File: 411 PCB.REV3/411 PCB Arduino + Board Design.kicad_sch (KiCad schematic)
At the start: 27 parts, among them J1 ICSP CONN, J3 Conn_01x04, J4 HEADER-1X770MIL, Q1 Q_NMOS_GDS, SW1 SW_SPST, SW2 SW_MEC_5E, U2 ATmega328P-P, Y1 8 MHz

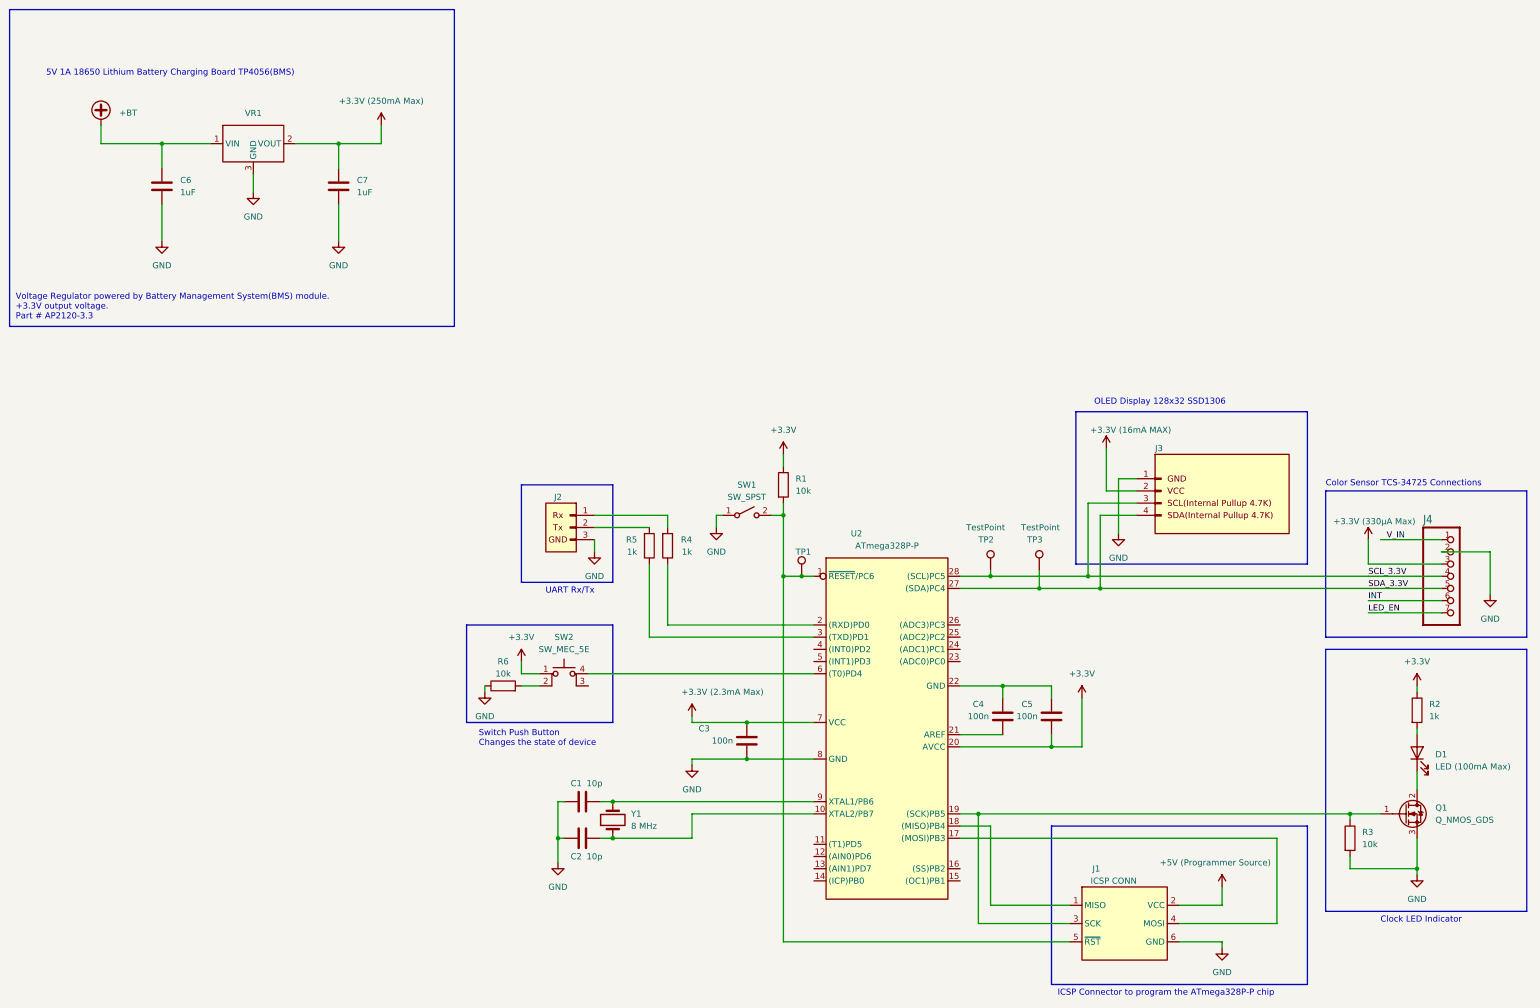
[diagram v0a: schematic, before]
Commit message: EEPROM, Debounce, more testpoints (#2)
* Create RGB_sensor_project.ino

Arduino projector, getting basics of the color sensor and display working (together).

* Removed RGB LED code and cleaned up code

* added LED connection for RGB Sensor

* starting to incorporate EEPROM

* Added EEPROM code and changed the pins for button and RGB Sensors LED. Also changed how the chip goes into calibration mode

* pins that work

* Fixed debounce error and added more test points to schematic
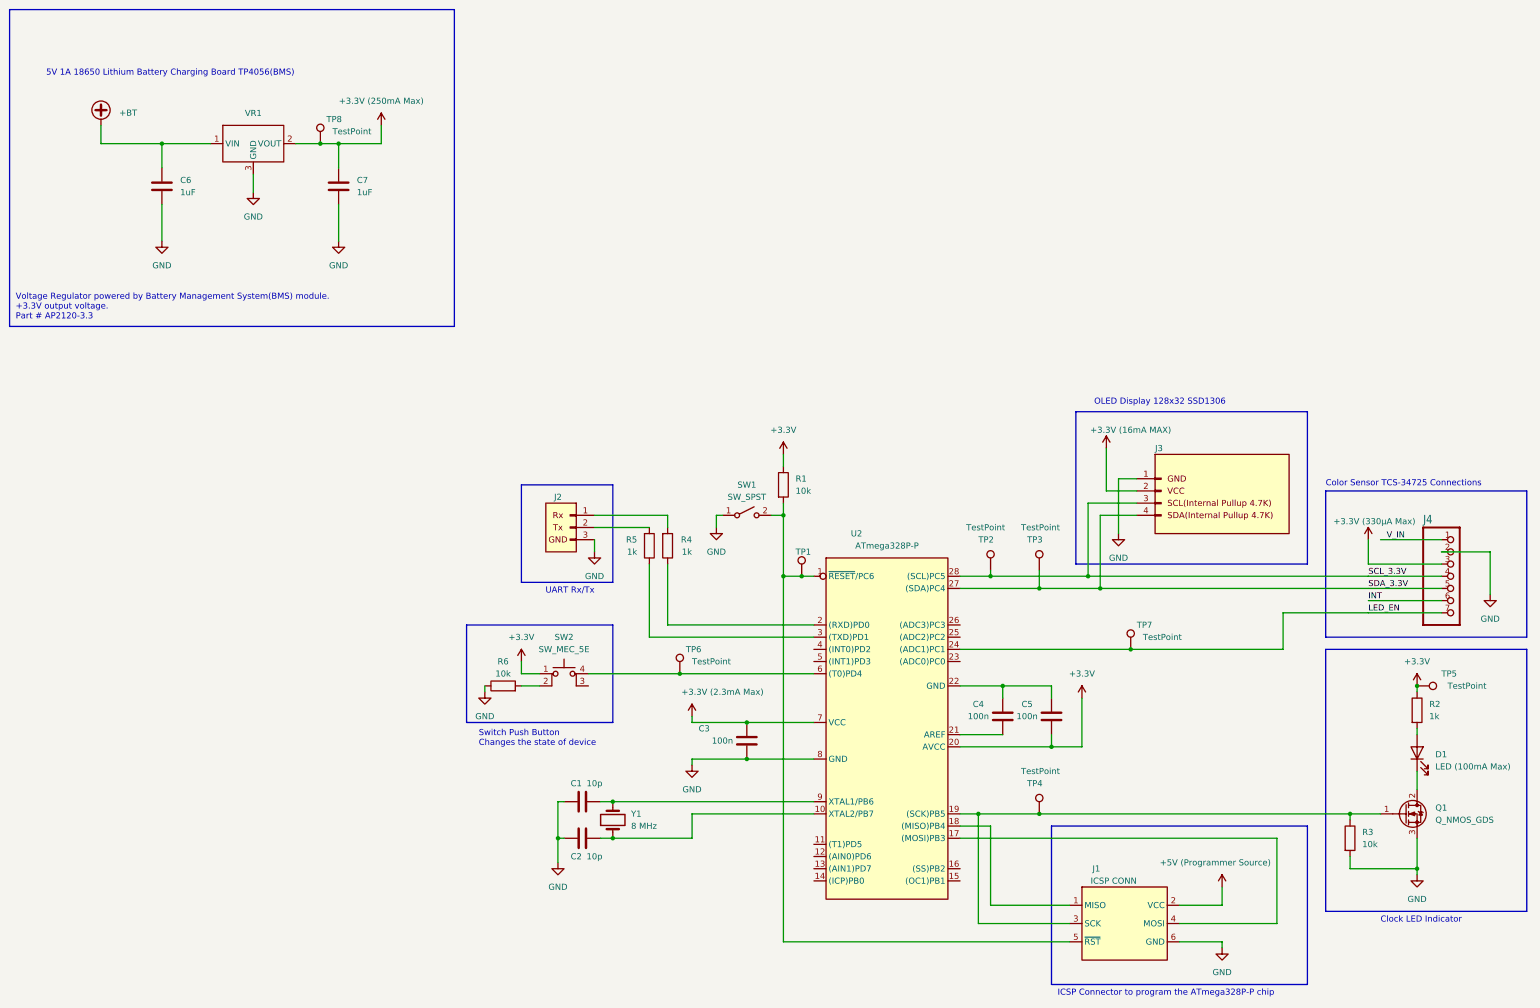
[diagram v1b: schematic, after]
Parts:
- added TP4, TP5, TP6, TP7, TP8: TestPoint, Connector_PinHeader_1.00mm:PinHeader_1x01_P1.00mm_Vertical, symbol Connector:TestPoint
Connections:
- net +3.3V: now also TP5.1, TP8.1
- net LED_EN: now also U2.24 ((ADC1)PC1), TP7.1
- net at SW2.4 (A), U2.6 ((T0)PD4): now also TP6.1
- net at J1.3 (SCK), Q1.1 (G), R3.1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: now also TP4.1
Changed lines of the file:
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@@
   (junction (at 132.08 99.06) (diameter 0) (color 0 0 0 0)
   )
+  (junction (at 393.7 212.09) (diameter 0) (color 0 0 0 0)
+  )
   (junction (at 261.62 176.53) (diameter 0) (color 0 0 0 0)
   )
+  (junction (at 165.1 99.06) (diameter 0) (color 0 0 0 0)
+  )
   (junction (at 261.62 189.23) (diameter 0) (color 0 0 0 0)
   )
+  (junction (at 334.01 204.47) (diameter 0) (color 0 0 0 0)
+  )
   (junction (at 379.73 238.76) (diameter 0) (color 0 0 0 0)
   )
   (junction (at 317.5 224.79) (diameter 0) (color 0 0 0 0)
   )
+  (junction (at 240.03 209.55) (diameter 0) (color 0 0 0 0)
+  )
   (junction (at 226.06 243.84) (diameter 0) (color 0 0 0 0)
   )
@@
   )
   (junction (at 325.12 189.23) (diameter 0) (color 0 0 0 0)
+  )
+  (junction (at 314.96 238.76) (diameter 0) (color 0 0 0 0)
   )
   (junction (at 168.91 99.06) (diameter 0) (color 0 0 0 0)
@@
     (stroke (width 0) (type default))
   )
-  (wire (pts (xy 302.26 238.76) (xy 379.73 238.76))
+  (wire (pts (xy 302.26 238.76) (xy 314.96 238.76))
     (stroke (width 0) (type default))
   )
@@
     (stroke (width 0) (type default))
   )
+  (wire (pts (xy 298.45 204.47) (xy 334.01 204.47))
+    (stroke (width 0) (type default))
+  )
   (wire (pts (xy 317.5 224.79) (xy 317.5 222.25))
     (stroke (width 0) (type default))
   )
+  (wire (pts (xy 165.1 99.06) (xy 168.91 99.06))
+    (stroke (width 0) (type default))
+  )
   (wire (pts (xy 226.06 236.22) (xy 267.97 236.22))
     (stroke (width 0) (type default))
   )
   (wire (pts (xy 168.91 111.76) (xy 168.91 119.38))
+    (stroke (width 0) (type default))
+  )
+  (wire (pts (xy 365.76 196.85) (xy 383.54 196.85))
     (stroke (width 0) (type default))
   )
@@
     (stroke (width 0) (type default))
   )
+  (wire (pts (xy 240.03 209.55) (xy 267.97 209.55))
+    (stroke (width 0) (type default))
+  )
   (wire (pts (xy 398.78 184.15) (xy 408.94 184.15))
     (stroke (width 0.1524) (type solid))
@@
     (stroke (width 0) (type default))
   )
-  (wire (pts (xy 160.02 99.06) (xy 168.91 99.06))
+  (wire (pts (xy 160.02 99.06) (xy 165.1 99.06))
     (stroke (width 0) (type default))
   )
   (wire (pts (xy 248.92 176.53) (xy 247.65 176.53))
+    (stroke (width 0) (type default))
+  )
+  (wire (pts (xy 334.01 204.47) (xy 365.76 204.47))
     (stroke (width 0) (type default))
   )
@@
     (stroke (width 0) (type default))
   )
-  (wire (pts (xy 220.98 209.55) (xy 267.97 209.55))
+  (wire (pts (xy 220.98 209.55) (xy 240.03 209.55))
     (stroke (width 0) (type default))
   )
@@
     (stroke (width 0) (type default))
   )
+  (wire (pts (xy 365.76 204.47) (xy 365.76 196.85))
+    (stroke (width 0) (type default))
+  )
   (wire (pts (xy 327.66 191.77) (xy 383.54 191.77))
     (stroke (width 0) (type default))
@@
   )
   (wire (pts (xy 393.7 220.98) (xy 393.7 222.25))
+    (stroke (width 0) (type default))
+  )
+  (wire (pts (xy 314.96 238.76) (xy 379.73 238.76))
     (stroke (width 0) (type default))
   )
@@
     )
   )
+  (symbol (lib_id "Connector:TestPoint") (at 334.01 204.47 0) (unit 1)
+    (in_bom yes) (on_board yes) (dnp no)
+    (property "Reference" "TP7" (at 335.28 199.39 0)
+      (effects (font (size 1.27 1.27)) (justify left))
+    )
+    (property "Value" "TestPoint" (at 336.55 201.93 0)
+      (effects (font (size 1.27 1.27)) (justify left))
+    )
+    (property "Footprint" "Connector_PinHeader_1.00mm:PinHeader_1x01_P1.00mm_Vertical" (at 339.09 204.47 0)
+      (effects (font (size 1.27 1.27)) hide)
+    )
+    (property "Datasheet" "~" (at 339.09 204.47 0)
+      (effects (font (size 1.27 1.27)) hide)
+    )
+    (pin "1")
+    (instances
+      (project "411 PCB Arduino + Board Design"
+        (path "/3b213592-ad28-4b80-bc7a-214b9fe026d8"
+          (reference "TP7") (unit 1)
+        )
+      )
+    )
+  )
   (symbol (lib_id "power:GND") (at 331.47 180.34 0) (unit 1)
     (in_bom yes) (on_board yes) (dnp no) (fields_autoplaced)
@@
     )
   )
+  (symbol (lib_id "Connector:TestPoint") (at 165.1 99.06 0) (unit 1)
+    (in_bom yes) (on_board yes) (dnp no)
+    (property "Reference" "TP8" (at 166.37 93.98 0)
+      (effects (font (size 1.27 1.27)) (justify left))
+    )
+    (property "Value" "TestPoint" (at 167.64 96.52 0)
+      (effects (font (size 1.27 1.27)) (justify left))
+    )
+    (property "Footprint" "Connector_PinHeader_1.00mm:PinHeader_1x01_P1.00mm_Vertical" (at 170.18 99.06 0)
+      (effects (font (size 1.27 1.27)) hide)
+    )
+    (property "Datasheet" "~" (at 170.18 99.06 0)
+      (effects (font (size 1.27 1.27)) hide)
+    )
+    (pin "1")
+    (instances
+      (project "411 PCB Arduino + Board Design"
+        (path "/3b213592-ad28-4b80-bc7a-214b9fe026d8"
+          (reference "TP8") (unit 1)
+        )
+      )
+    )
+  )
   (symbol (lib_id "power:GND") (at 408.94 193.04 0) (unit 1)
     (in_bom yes) (on_board yes) (dnp no) (fields_autoplaced)
@@
         (path "/3b213592-ad28-4b80-bc7a-214b9fe026d8"
           (reference "#PWR032") (unit 1)
+        )
+      )
+    )
+  )
+  (symbol (lib_id "Connector:TestPoint") (at 240.03 209.55 0) (unit 1)
+    (in_bom yes) (on_board yes) (dnp no)
+    (property "Reference" "TP6" (at 241.3 204.47 0)
+      (effects (font (size 1.27 1.27)) (justify left))
+    )
+    (property "Value" "TestPoint" (at 242.57 207.01 0)
+      (effects (font (size 1.27 1.27)) (justify left))
+    )
+    (property "Footprint" "Connector_PinHeader_1.00mm:PinHeader_1x01_P1.00mm_Vertical" (at 245.11 209.55 0)
+      (effects (font (size 1.27 1.27)) hide)
+    )
+    (property "Datasheet" "~" (at 245.11 209.55 0)
+      (effects (font (size 1.27 1.27)) hide)
+    )
+    (pin "1")
+    (instances
+      (project "411 PCB Arduino + Board Design"
+        (path "/3b213592-ad28-4b80-bc7a-214b9fe026d8"
+          (reference "TP6") (unit 1)
         )
       )
@@
     )
   )
+  (symbol (lib_id "Connector:TestPoint") (at 393.7 212.09 270) (unit 1)
+    (in_bom yes) (on_board yes) (dnp no)
+    (property "Reference" "TP5" (at 398.78 209.55 90)
+      (effects (font (size 1.27 1.27)) (justify left))
+    )
+    (property "Value" "TestPoint" (at 400.05 212.09 90)
+      (effects (font (size 1.27 1.27)) (justify left))
+    )
+    (property "Footprint" "Connector_PinHeader_1.00mm:PinHeader_1x01_P1.00mm_Vertical" (at 393.7 217.17 0)
+      (effects (font (size 1.27 1.27)) hide)
+    )
+    (property "Datasheet" "~" (at 393.7 217.17 0)
+      (effects (font (size 1.27 1.27)) hide)
+    )
+    (pin "1")
+    (instances
+      (project "411 PCB Arduino + Board Design"
+        (path "/3b213592-ad28-4b80-bc7a-214b9fe026d8"
+          (reference "TP5") (unit 1)
+        )
+      )
+    )
+  )
   (symbol (lib_id "power:GND") (at 353.06 266.7 0) (unit 1)
     (in_bom yes) (on_board yes) (dnp no)
@@
         )
       )
+    )
+  )
+  (symbol (lib_id "Connector:TestPoint") (at 314.96 238.76 0) (unit 1)
+    (in_bom yes) (on_board yes) (dnp no)
+    (property "Reference" "TP4" (at 312.42 232.41 0)
+      (effects (font (size 1.27 1.27)) (justify left))
+    )
+    (property "Value" "TestPoint" (at 311.15 229.87 0)
+      (effects (font (size 1.27 1.27)) (justify left))
+    )
+    (property "Footprint" "Connector_PinHeader_1.00mm:PinHeader_1x01_P1.00mm_Vertical" (at 320.04 238.76 0)
+      (effects (font (size 1.27 1.27)) hide)
+    )
+    (property "Datasheet" "~" (at 320.04 238.76 0)
+      (effects (font (size 1.27 1.27)) hide)
+    )
+    (pin "1")
+    (instances
+      (project "411 PCB Arduino + Board Design"
+        (path "/3b213592-ad28-4b80-bc7a-214b9fe026d8"
+          (reference "TP4") (unit 1)
+        )
+      )
